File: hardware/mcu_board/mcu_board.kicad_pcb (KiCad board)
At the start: 2 copper layers, 98.4 x 48 mm, 17 parts, among them J1 TANK-TOP, J2 TANK-BOTTOM, J3 COLD, J4 DISPLAY, J5 RTC, J6 Conn_01x02_Pin, J7 MCU, SW2 RotaryEncoder_Switch, U1 ESP32-S3-DevKitC, U12 DHT11

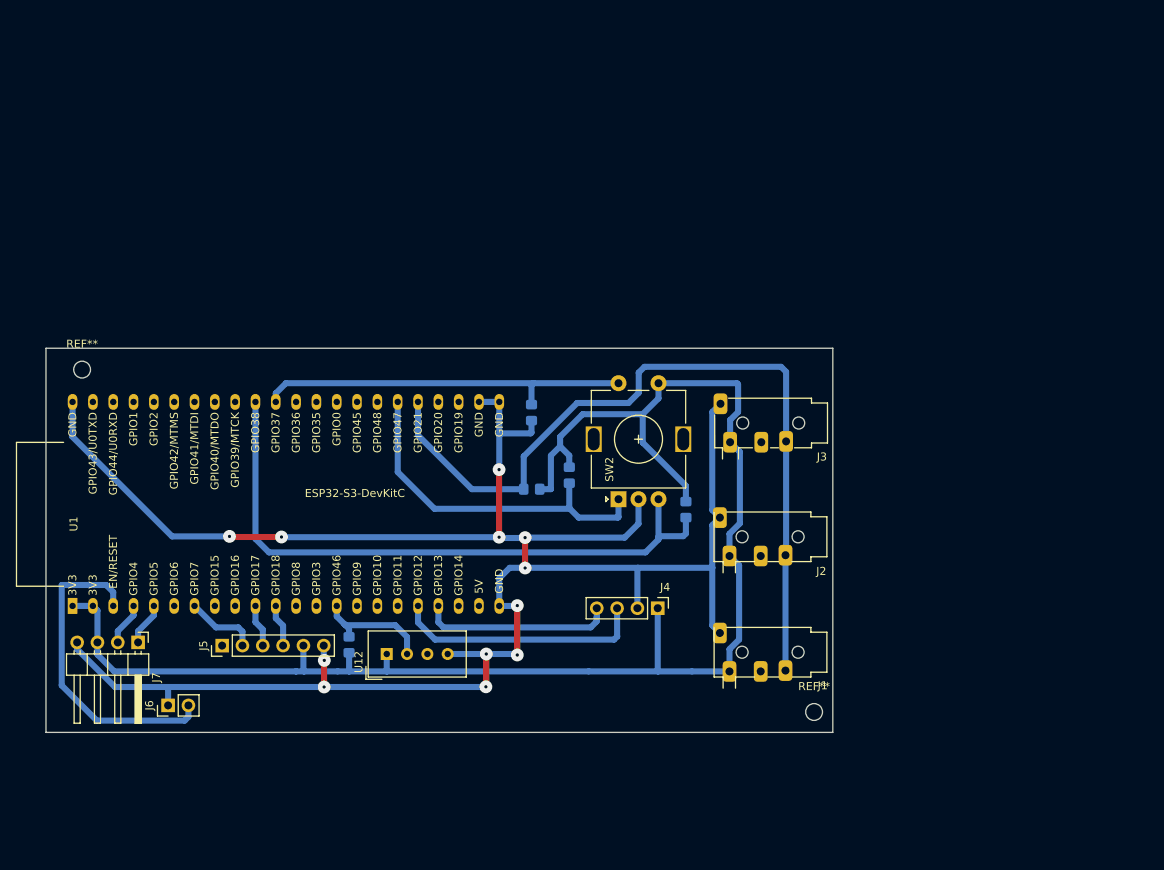
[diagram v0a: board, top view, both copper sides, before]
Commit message: Refactored PCBs for v2. See README
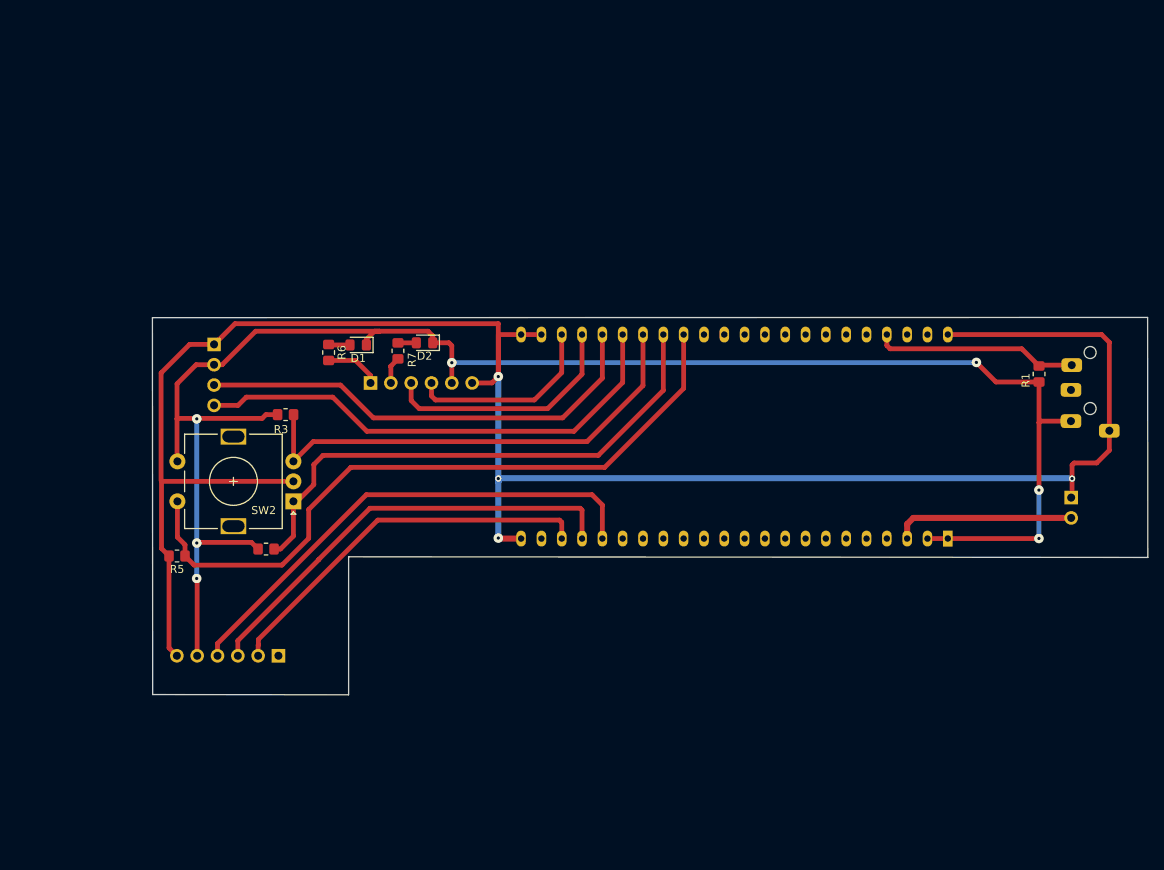
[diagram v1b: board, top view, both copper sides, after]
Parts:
- removed J1: TANK-TOP, Connector_Audio:Jack_3.5mm_PJ320D_Horizontal_NG
- removed J2: TANK-BOTTOM, Connector_Audio:Jack_3.5mm_PJ320D_Horizontal_NG
- removed R4: 4k7, Resistor_SMD:R_0805_2012Metric_Pad1.20x1.40mm_HandSolder
- removed REF** (x2): MountingHole_2.1mm, MountingHole:MountingHole_2.1mm
- removed U12: DHT11, Sensor:Aosong_DHT11_5.5x12.0_P2.54mm
- added D1: LED, Diode_SMD:D_0805_2012Metric_Pad1.15x1.40mm_HandSolder, F.Cu at (57.0, 74.8)
- added D2: LED, Diode_SMD:D_0805_2012Metric_Pad1.15x1.40mm_HandSolder, F.Cu at (65.3, 74.5)
- added R6: 330R, Resistor_SMD:R_0805_2012Metric_Pad1.20x1.40mm_HandSolder, F.Cu at (53.3, 75.8)
- added R7: 330R, Resistor_SMD:R_0805_2012Metric_Pad1.20x1.40mm_HandSolder, F.Cu at (62.0, 75.6)
- J3, J4, J5, J6, U1: moved to B.Cu
- J7: footprint Connector_PinHeader_2.54mm:PinHeader_1x04_P2.54mm_Horizontal -> Connector_PinHeader_2.54mm:PinHeader_1x06_P2.54mm_Horizontal; moved to B.Cu
- R1, R2, R3, R5: moved to F.Cu
- moved J6 115.8 mm to (146.2, 93.9), turned to 180 degrees
- moved U1 109.7 mm to (130.7, 99.0)
- moved R1 65.0 mm to (142.1, 78.5), turned to -90 degrees
- moved J4 64.5 mm to (39.0, 74.8), turned to 180 degrees
- moved R3 51.4 mm to (48.0, 83.5), turned to 0 degrees
- moved R5 47.8 mm to (34.4, 101.2), turned to 180 degrees
- moved J7 43.5 mm to (58.6, 79.6)
- moved J3 41.4 mm to (148.5, 80.5), turned to -90 degrees
- moved SW2 40.6 mm to (48.9, 94.4), turned to 180 degrees
- moved R2 39.0 mm to (45.5, 100.3), turned to 0 degrees
- moved J5 7.15 mm to (47.1, 113.7)
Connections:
- J4 pad 1: +3.3V -> GND
- J4 pad 2: GND -> +3.3V
- J7 pad 1: RELAY_BOTTOM -> LED_BOTTOM
- J7 pad 2: RELAY_TOP -> LED_TOP
- J7 pad 3: +3.3V -> RELAY_BOTTOM
- J7 pad 4: GND -> RELAY_TOP
- U1 pad 10: RTC_SCK -> unconnected-(U1-GPIO17/ADC2_CH6-Pad10)
- U1 pad 11: RTC_SDA -> unconnected-(U1-GPIO18/ADC2_CH7-Pad11)
- U1 pad 14: DHT_DATA -> unconnected-(U1-GPIO46-Pad14)
- U1 pad 18: DISPLAY_SCL -> RTC_SDA
- U1 pad 19: DISPLAY_SDA -> RTC_SCK
- U1 pad 20: unconnected-(U1-GPIO14/ADC2_CH3-Pad20) -> RTC_SQW
- U1 pad 25: unconnected-(U1-GPIO19/USB_D--Pad25) -> RELAY_TOP
- U1 pad 26: unconnected-(U1-GPIO20/USB_D+-Pad26) -> RELAY_BOTTOM
- U1 pad 27: WATERTEMP_DATA -> DISPLAY_SCL
- U1 pad 28: ROT_CLK -> DISPLAY_SDA
- U1 pad 29: unconnected-(U1-GPIO48-Pad29) -> ROT_DT
- U1 pad 30: unconnected-(U1-GPIO45-Pad30) -> ROT_CLK
- U1 pad 31: unconnected-(U1-GPIO0-Pad31) -> ROT_SW
- U1 pad 34: ROT_SW -> unconnected-(U1-GPIO37-Pad34)
- U1 pad 35: ROT_DT -> unconnected-(U1-GPIO38-Pad35)
- U1 pad 4: RELAY_TOP -> unconnected-(U1-GPIO4/ADC1_CH3-Pad4)
- U1 pad 41: unconnected-(U1-GPIO1/ADC1_CH0-Pad41) -> WATERTEMP_DATA
- U1 pad 5: RELAY_BOTTOM -> unconnected-(U1-GPIO5/ADC1_CH4-Pad5)
- U1 pad 7: RTC_SQW -> unconnected-(U1-GPIO7/ADC1_CH6-Pad7)
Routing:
- net WATERTEMP_DATA: track 100.8 -> 25.6 mm
- net RTC_SDA: track 5.34 -> 62.1 mm
- net RTC_SCK: track 5.34 -> 55.4 mm
- net ROT_SW: track 47.7 -> 88.0 mm
- net RTC_SQW: track 9.08 -> 48.3 mm
- net DISPLAY_SDA: track 24.1 -> 61.8 mm
- net DISPLAY_SCL: track 31.6 -> 57.8 mm
- net RELAY_BOTTOM: track 5.37 -> 30.7 mm
- net +3.3V: track 194.0 -> 218.0 mm, vias 0 -> 7
- net ROT_CLK: track 44.2 -> 67.9 mm
- net ROT_DT: track 79.0 -> 59.9 mm
- net RELAY_TOP: track 5.37 -> 24.3 mm
- net RESET: track 40.4 -> 22.6 mm
- net DHT_DATA: track 15.1 -> 0.00 mm
- net LED_BOTTOM: track 0.00 -> 6.95 mm
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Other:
- board size 98.4 x 48 mm -> 124.4 x 47.2 mm

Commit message: v2 layout changes to fit in bax
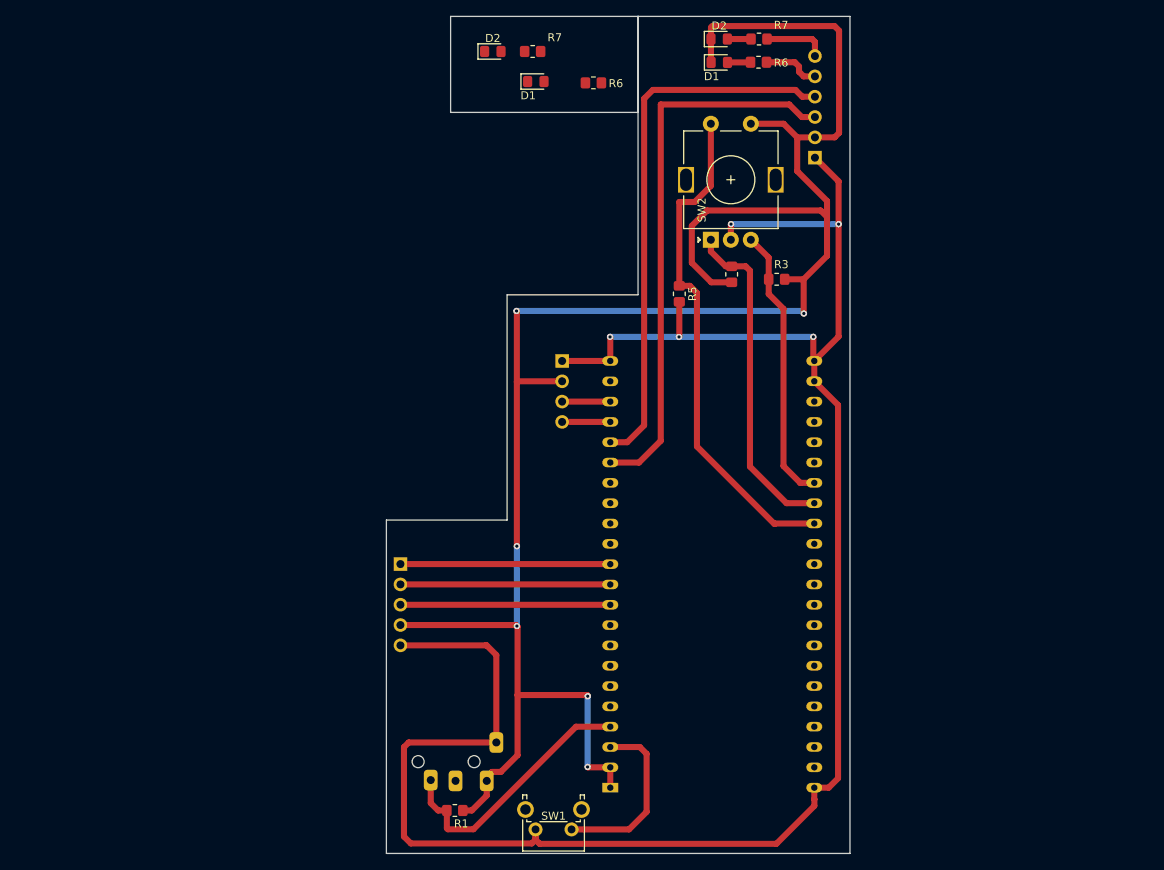
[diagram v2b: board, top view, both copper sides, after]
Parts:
- removed J6: Conn_01x02_Pin, Connector_PinHeader_2.54mm:PinHeader_1x02_P2.54mm_Vertical
- added D1: LED, Diode_SMD:D_0805_2012Metric_Pad1.15x1.40mm_HandSolder, F.Cu at (79.2, 41.9)
- added D2: LED, Diode_SMD:D_0805_2012Metric_Pad1.15x1.40mm_HandSolder, F.Cu at (73.9, 38.1)
- added R6: 330R, Resistor_SMD:R_0805_2012Metric_Pad1.20x1.40mm_HandSolder, F.Cu at (86.4, 42.1)
- added R7: 330R, Resistor_SMD:R_0805_2012Metric_Pad1.20x1.40mm_HandSolder, F.Cu at (78.8, 38.1)
- added SW1: RESET, Button_Switch_THT:SW_Tactile_SPST_Angled_PTS645Vx39-2LFS, F.Cu at (83.7, 135.4)
- J5: footprint Connector_PinHeader_2.54mm:PinHeader_1x06_P2.54mm_Vertical -> Connector_PinHeader_2.54mm:PinHeader_1x05_P2.54mm_Vertical
- moved J3 91.8 mm to (69.3, 126.9), turned to 0 degrees
- moved R1 91.2 mm to (69.1, 133.0), turned to 0 degrees
- moved R5 70.8 mm to (97.2, 68.4), turned to -90 degrees
- moved R2 67.6 mm to (103.7, 66.0), turned to 90 degrees
- moved R6 64.8 mm to (107.1, 39.5), turned to 0 degrees
- moved R3 63.7 mm to (109.3, 66.6), turned to 180 degrees
- moved J7 62.3 mm to (114.1, 51.4), turned to 0 degrees
- moved SW2 61.6 mm to (101.1, 61.7), turned to 90 degrees
- moved R7 59.6 mm to (107.1, 36.6), turned to 0 degrees
- moved D1 57.3 mm to (102.2, 39.5), turned to 0 degrees
- moved D2 52.9 mm to (102.2, 36.6), turned to 0 degrees
- moved U1 52.4 mm to (88.5, 130.2), turned to 0 degrees
- moved J4 43.6 mm to (82.5, 76.8)
- moved J5 19.1 mm to (62.3, 102.2), turned to 180 degrees
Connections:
- J5 pad 1: unconnected-(J5-Pin_1-Pad1) -> RTC_SQW
- J5 pad 2: RTC_SQW -> RTC_SCK
- J5 pad 3: RTC_SCK -> RTC_SDA
- J5 pad 4: RTC_SDA -> +3.3V
- J5 pad 5: +3.3V -> GND
- J7 pad 1: LED_BOTTOM -> GND
- J7 pad 2: LED_TOP -> +3.3V
- J7 pad 5: +3.3V -> LED_BOTTOM
- J7 pad 6: GND -> LED_TOP
- U1 pad 10: unconnected-(U1-GPIO17/ADC2_CH6-Pad10) -> RTC_SDA
- U1 pad 11: unconnected-(U1-GPIO18/ADC2_CH7-Pad11) -> RTC_SCK
- U1 pad 12: unconnected-(U1-GPIO8/ADC1_CH7-Pad12) -> RTC_SQW
- U1 pad 17: unconnected-(U1-GPIO11/ADC2_CH0-Pad17) -> RELAY_BOTTOM
- U1 pad 18: RTC_SDA -> RELAY_TOP
- U1 pad 19: RTC_SCK -> DISPLAY_SDA
- U1 pad 20: RTC_SQW -> DISPLAY_SCL
- U1 pad 25: RELAY_TOP -> unconnected-(U1-GPIO19/USB_D--Pad25)
- U1 pad 26: RELAY_BOTTOM -> unconnected-(U1-GPIO20/USB_D+-Pad26)
- U1 pad 27: DISPLAY_SCL -> unconnected-(U1-GPIO21-Pad27)
- U1 pad 28: DISPLAY_SDA -> unconnected-(U1-GPIO47-Pad28)
- U1 pad 4: unconnected-(U1-GPIO4/ADC1_CH3-Pad4) -> WATERTEMP_DATA
- U1 pad 41: WATERTEMP_DATA -> unconnected-(U1-GPIO1/ADC1_CH0-Pad41)
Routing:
- net DISPLAY_SDA: track 61.8 -> 6.02 mm
- net DISPLAY_SCL: track 57.8 -> 6.02 mm
- net RELAY_TOP: track 24.3 -> 68.5 mm
- net RELAY_BOTTOM: track 30.7 -> 69.4 mm
- net RTC_SDA: track 62.1 -> 26.2 mm
- net +3.3V: track 218.0 -> 247.7 mm, vias 7 -> 6
- net RTC_SCK: track 55.4 -> 26.2 mm
- net ROT_CLK: track 67.9 -> 41.8 mm
- net ROT_DT: track 59.9 -> 34.7 mm
- net ROT_SW: track 88.0 -> 63.5 mm
- net RTC_SQW: track 48.3 -> 26.2 mm
- net GND: track 255.9 -> 246.1 mm, vias 4 -> 5
- net WATERTEMP_DATA: track 25.6 -> 33.3 mm
- net LED_TOP: track 3.40 -> 7.91 mm
- net Net-(D2-A): track 2.30 -> 2.95 mm
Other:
- board size 124.4 x 47.2 mm -> 58 x 104.6 mm

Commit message: Laypout tweaks to fit case
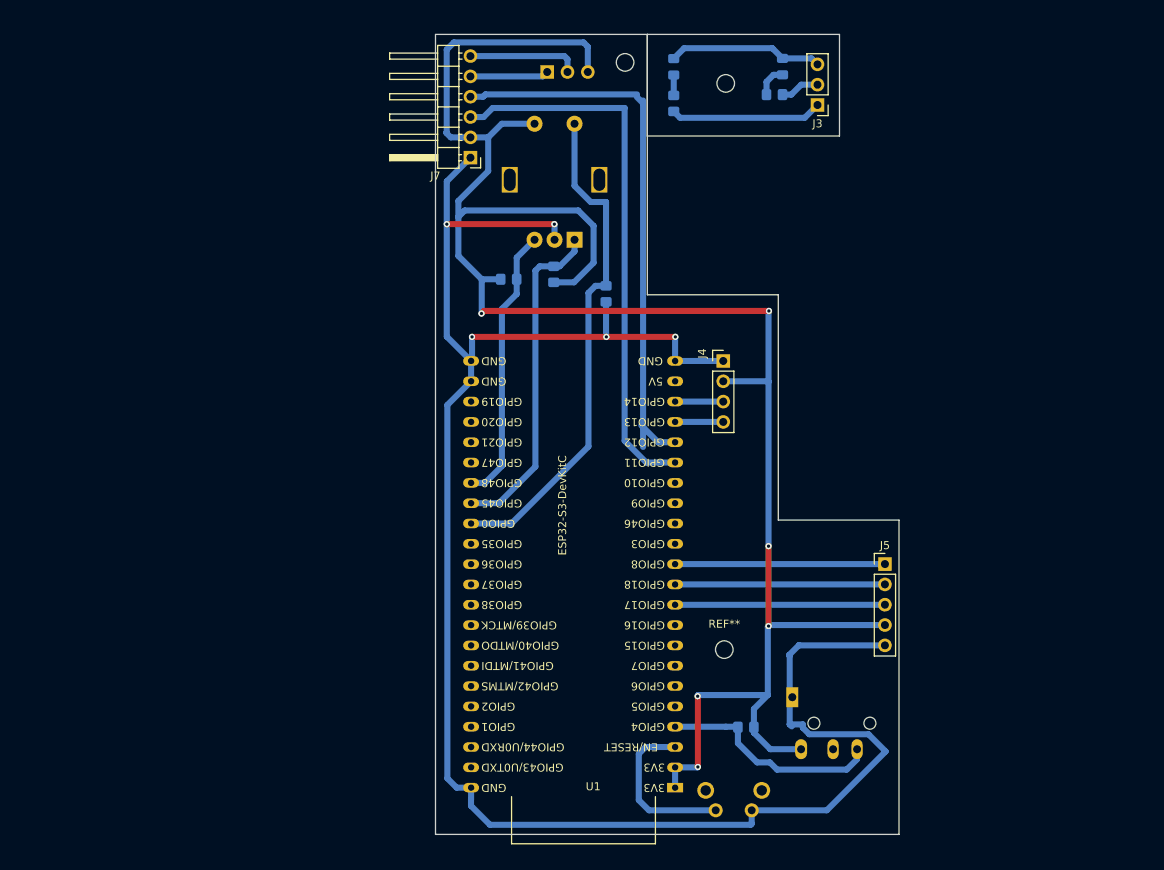
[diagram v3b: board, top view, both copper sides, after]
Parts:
- removed the D1 at (102.2, 39.5)
- removed the D2 at (102.2, 36.6)
- removed the R6 at (107.1, 39.5)
- removed the R7 at (107.1, 36.6)
- added J1: TEMP, Connector_Audio_2:Jack_3.5mm_PJ320D_Horizontal, B.Cu at (116.2, 122.1)
- added J2: LEDS_OUT, Connector_PinHeader_2.54mm:PinHeader_1x03_P2.54mm_Vertical, B.Cu at (80.7, 40.7)
- added REF**: MountingHole_2.2mm_M2, MountingHole:MountingHole_2.2mm_M2, F.Cu at (102.8, 112.9)
- added REF**: MountingHole_2.2mm_M2, MountingHole:MountingHole_2.2mm_M2, F.Cu at (90.4, 39.5)
- added REF**: MountingHole_2.2mm_M2, MountingHole:MountingHole_2.2mm_M2, F.Cu at (103.0, 42.1)
- D1, D2, R1, R2, R3, R5, R6, R7, SW1, SW2: moved to B.Cu
- J3: value COLD -> LEDS_IN; footprint Connector_Audio:Jack_3.5mm_PJ320D_Horizontal_NG -> Connector_PinHeader_2.54mm:PinHeader_1x03_P2.54mm_Vertical; moved to F.Cu
- J4, J5, J7, U1: moved to F.Cu
- moved J3 93.7 mm to (114.5, 44.8), turned to 180 degrees
- moved J5 60.6 mm to (122.9, 102.2), turned to 0 degrees
- moved J7 43.1 mm to (71.1, 51.4), turned to 180 degrees
- moved R1 37.8 mm to (105.5, 122.6)
- moved D2 36.3 mm to (110.1, 40.0), turned to -90 degrees
- moved R3 33.5 mm to (75.8, 66.6), turned to 0 degrees
- moved R7 30.7 mm to (109.1, 43.5)
- moved R2 22.2 mm to (81.5, 66.0)
- moved J4 20.1 mm to (102.7, 76.8), turned to 0 degrees
- moved SW1 18.2 mm to (101.7, 133.0), turned to 0 degrees
- moved D1 17.3 mm to (96.5, 40.0), turned to -90 degrees
- moved SW2 17.0 mm to (84.1, 61.7)
- moved R6 10.4 mm to (96.5, 44.6), turned to -90 degrees
- moved R5 9.16 mm to (88.0, 68.4)
- moved U1 8.10 mm to (96.7, 130.2), turned to 180 degrees
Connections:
- D1 pad 1: +3.3V -> Net-(D1-K)
- D2 pad 1: +3.3V -> Net-(D1-K)
- R6 pad 2: LED_BOTTOM -> Net-(J3-Pin_1)
- R7 pad 2: LED_TOP -> Net-(J3-Pin_2)
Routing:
- net Net-(D1-K): track 0.00 -> 19.3 mm
- net Net-(J3-Pin_1): track 0.00 -> 19.0 mm
- net GND: track 246.1 -> 237.1 mm
- net +3.3V: track 247.7 -> 239.5 mm
- net LED_TOP: track 7.91 -> 13.9 mm
- net WATERTEMP_DATA: track 33.3 -> 27.9 mm
- net Net-(J3-Pin_2): track 0.00 -> 4.89 mm
- net LED_BOTTOM: track 7.19 -> 9.82 mm
- net RELAY_TOP: track 68.5 -> 70.8 mm
- net RESET: track 22.4 -> 20.8 mm
- net Net-(D2-A): track 2.95 -> 3.96 mm
- net RELAY_BOTTOM: track 69.4 -> 68.8 mm
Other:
- board size 58 x 104.6 mm -> 57.9 x 100 mm

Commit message: v2 Boards for fabrication
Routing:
- net GND: track 237.1 -> 240.5 mm
- net RELAY_TOP: track 70.8 -> 68.8 mm
- net WATERTEMP_DATA: track 27.9 -> 29.8 mm
- added copper zone on B.Cu, net (none)
